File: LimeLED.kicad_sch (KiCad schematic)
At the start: 16 parts, among them CN1 HB9500-3, CN2 HB9500-3, U1 ESP32-DEVKITC-32D, U2 TPSM863257RDXR, U3 220k, U4 SN74AHCT125N

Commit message: add input protection and plotted schematic
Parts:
- added C7: 470uF 25v, Capacitor_THT:CP_Radial_D8.0mm_P3.50mm, symbol Device:C_Polarized
- added C8: 100nF 25v, Capacitor_SMD:C_0402_1005Metric, symbol Device:C_Small
- added F2: 500mA, easyeda2kicad:F1206, symbol easyeda2kicad:SMD1206B050TF_15
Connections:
- net +12V: now also F1.2, C7.1, C8.1, F2.2; no longer C1.2, C2.1, CN2.1, CN2.2, CN2.3, R1.1, U2.1 (VIN)
- net GND: now also C7.2, C8.2
- net at F1.1: now also CN2.1, CN2.2, CN2.3
- new net: C1.2, C2.1, F2.1, R1.1, U2.1 (VIN)
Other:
- moved on the sheet: CN1, CN2, F1

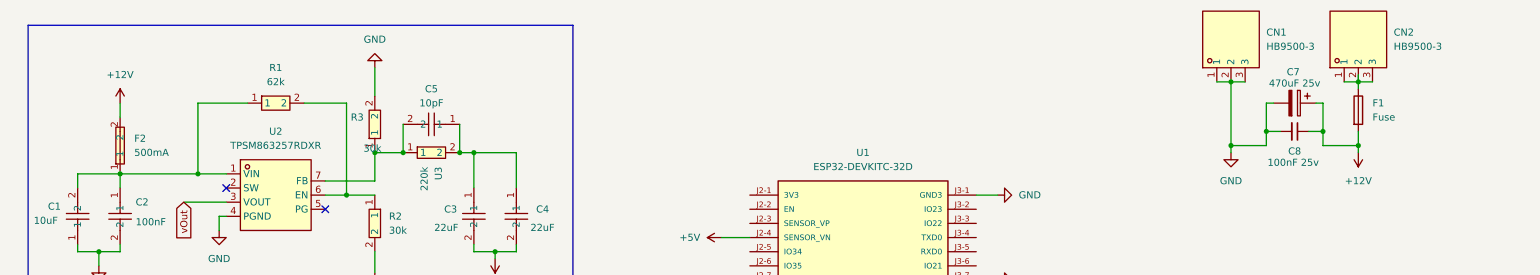
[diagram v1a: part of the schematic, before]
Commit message: wire connections
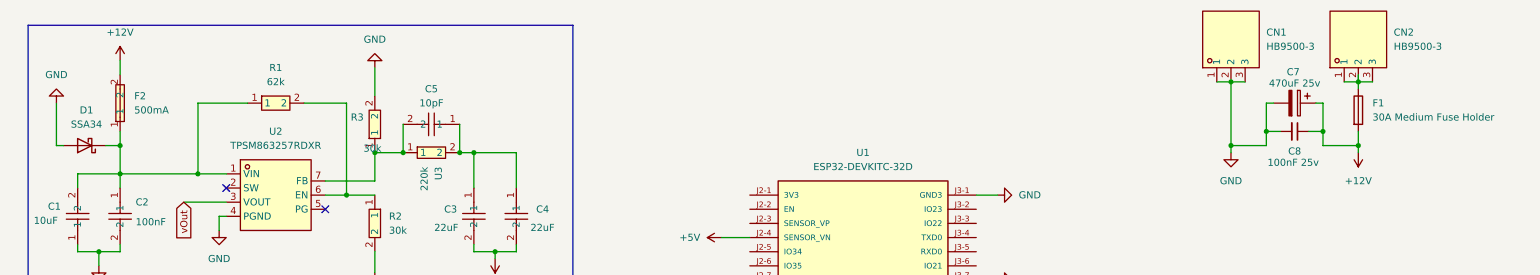
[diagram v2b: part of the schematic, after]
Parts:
- added D1: SSA34, Diode_SMD:D_SMA, symbol Device:D_Schottky
- F1: value Fuse -> 30A Medium Fuse Holder
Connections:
- net GND: now also D1.2 (A)
- net at C1.2, C2.1, F2.1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: now also D1.1 (K)
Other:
- moved on the sheet: F2
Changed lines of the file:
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@@
+	)
+	(junction
+		(at 35.56 43.18)
+		(diameter 0)
+		(color 0 0 0 0)
 	)
 	(junction
@@
 	(wire
 		(pts
+			(xy 24.13 43.18) (xy 25.4 43.18)
+		)
+		(stroke
+			(width 0)
+			(type default)
+		)
+	)
+	(wire
+		(pts
 			(xy 257.81 31.75) (xy 260.35 31.75)
 		)
@@
 	(wire
 		(pts
+			(xy 33.02 43.18) (xy 35.56 43.18)
+		)
+		(stroke
+			(width 0)
+			(type default)
+		)
+	)
+	(wire
+		(pts
 			(xy 106.68 60.96) (xy 106.68 62.23)
 		)
@@
 	(wire
 		(pts
+			(xy 35.56 27.94) (xy 35.56 30.48)
+		)
+		(stroke
+			(width 0)
+			(type default)
+		)
+	)
+	(wire
+		(pts
 			(xy 38.1 105.41) (xy 48.26 105.41)
 		)
@@
 	(wire
 		(pts
-			(xy 35.56 35.56) (xy 35.56 38.1)
-		)
-		(stroke
-			(width 0)
-			(type default)
-		)
-	)
-	(wire
-		(pts
 			(xy 73.66 105.41) (xy 78.74 105.41)
 		)
@@
 	(wire
 		(pts
+			(xy 24.13 35.56) (xy 24.13 43.18)
+		)
+		(stroke
+			(width 0)
+			(type default)
+		)
+	)
+	(wire
+		(pts
+			(xy 35.56 40.64) (xy 35.56 43.18)
+		)
+		(stroke
+			(width 0)
+			(type default)
+		)
+	)
+	(wire
+		(pts
 			(xy 49.53 35.56) (xy 58.42 35.56)
 		)
@@
 		(pts
 			(xy 43.18 102.87) (xy 43.18 110.49)
+		)
+		(stroke
+			(width 0)
+			(type default)
+		)
+	)
+	(wire
+		(pts
+			(xy 35.56 43.18) (xy 35.56 48.26)
 		)
 		(stroke
@@
 	(symbol
 		(lib_id "easyeda2kicad:SMD1206B050TF_15")
-		(at 35.56 43.18 90)
+		(at 35.56 35.56 90)
 		(unit 1)
 		(exclude_from_sim no)
@@
 		(fields_autoplaced yes)
 		(property "Reference" "F2"
-			(at 38.1 41.9099 90)
+			(at 38.1 34.2899 90)
 			(effects
 				(font
@@
 		)
 		(property "Value" "500mA"
-			(at 38.1 44.4499 90)
+			(at 38.1 36.8299 90)
 			(effects
 				(font
@@
 		)
 		(property "Footprint" "easyeda2kicad:F1206"
-			(at 43.18 43.18 0)
+			(at 43.18 35.56 0)
 			(effects
 				(font
@@
 		)
 		(property "Datasheet" "https://lcsc.com/product-detail/Surface-Mount-Fuses_0-5A-15V_C170165.html"
-			(at 45.72 43.18 0)
+			(at 45.72 35.56 0)
 			(effects
 				(font
@@
 		)
 		(property "Description" ""
-			(at 35.56 43.18 0)
+			(at 35.56 35.56 0)
 			(effects
 				(font
@@
 		)
 		(property "LCSC Part" "C170165"
-			(at 48.26 43.18 0)
+			(at 48.26 35.56 0)
 			(effects
 				(font
@@
 			)
 		)
-		(property "Value" "Fuse"
+		(property "Value" "30A Medium Fuse Holder"
 			(at 260.35 38.0999 0)
 			(effects
@@
 			)
 		)
-		(property "Description" "Fuse"
+		(property "Description" "Fuse https://www.aliexpress.com/item/33046363182.html?aff_fcid=27f0e0a0b700496bbda647752beed212-1654215773694-03622-_9iUXVp&tt=CPS_NORMAL&aff_fsk=_9iUXVp&afSmartRedirect=y&aff_fcid=e5dba592f4134194b19f09bf35b90000-1724109345417-07103-_9IbWU1&tt=CPS_NORMAL&aff_fsk=_9IbWU1&aff_platform=portals-tool&aff_trace_key=e5dba592f4134194b19f09bf35b90000-1724109345417-07103-_9IbWU1&afSmartRedirect=y"
 			(at 257.81 36.83 0)
 			(effects
@@
 	)
 	(symbol
+		(lib_id "Device:D_Schottky")
+		(at 29.21 43.18 180)
+		(unit 1)
+		(exclude_from_sim no)
+		(in_bom yes)
+		(on_board yes)
+		(dnp no)
+		(fields_autoplaced yes)
+		(property "Reference" "D1"
+			(at 29.5275 36.83 0)
+			(effects
+				(font
+					(size 1.27 1.27)
+				)
+			)
+		)
+		(property "Value" "SSA34"
+			(at 29.5275 39.37 0)
+			(effects
+				(font
+					(size 1.27 1.27)
+				)
+			)
+		)
+		(property "Footprint" "Diode_SMD:D_SMA"
+			(at 29.21 43.18 0)
+			(effects
+				(font
+					(size 1.27 1.27)
+				)
+				(hide yes)
+			)
+		)
+		(property "Datasheet" "~"
+			(at 29.21 43.18 0)
+			(effects
+				(font
+					(size 1.27 1.27)
+				)
+				(hide yes)
+			)
+		)
+		(property "Description" "Schottky diode"
+			(at 29.21 43.18 0)
+			(effects
+				(font
+					(size 1.27 1.27)
+				)
+				(hide yes)
+			)
+		)
+		(property "LCSC Part" "C5563753"
+			(at 29.21 43.18 0)
+			(effects
+				(font
+					(size 1.27 1.27)
+				)
+				(hide yes)
+			)
+		)
+		(pin "2"
+		)
+		(pin "1"
+		)
+		(instances
+			(project ""
+				(path "/8cd5c59d-c520-41d4-b0dd-a55cfcffecd3"
+					(reference "D1")
+					(unit 1)
+				)
+			)
+		)
+	)
+	(symbol
 		(lib_id "power:GND")
 		(at 234.95 44.45 0)
@@
 	(symbol
 		(lib_id "power:+12V")
-		(at 35.56 35.56 0)
+		(at 35.56 27.94 0)
 		(unit 1)
 		(exclude_from_sim no)
@@
 		(fields_autoplaced yes)
 		(property "Reference" "#PWR01"
-			(at 35.56 39.37 0)
+			(at 35.56 31.75 0)
 			(effects
 				(font
@@
 		)
 		(property "Value" "+12V"
-			(at 35.56 30.48 0)
+			(at 35.56 22.86 0)
 			(effects
 				(font
@@
 		)
 		(property "Footprint" ""
-			(at 35.56 35.56 0)
+			(at 35.56 27.94 0)
 			(effects
 				(font
@@
 		)
 		(property "Datasheet" ""
-			(at 35.56 35.56 0)
+			(at 35.56 27.94 0)
 			(effects
 				(font
@@
 		)
 		(property "Description" "Power symbol creates a global label with name \"+12V\""
-			(at 35.56 35.56 0)
+			(at 35.56 27.94 0)
 			(effects
 				(font
@@
 					(unit 1)
 				)
+			)
+		)
+	)
+	(symbol
+		(lib_id "power:GND")
+		(at 24.13 35.56 180)
+		(unit 1)
+		(exclude_from_sim no)
+		(in_bom yes)
+		(on_board yes)
+		(dnp no)
+		(fields_autoplaced yes)
+		(property "Reference" "#PWR016"
+			(at 24.13 29.21 0)
+			(effects
+				(font
+					(size 1.27 1.27)
+				)
+				(hide yes)
+			)
+		)
+		(property "Value" "GND"
+			(at 24.13 30.48 0)
+			(effects
+				(font
+					(size 1.27 1.27)
+				)
+			)
+		)
+		(property "Footprint" ""
+			(at 24.13 35.56 0)
+			(effects
+				(font
+					(size 1.27 1.27)
+				)
+				(hide yes)
+			)
+		)
+		(property "Datasheet" ""
+			(at 24.13 35.56 0)
+			(effects
+				(font
+					(size 1.27 1.27)
+				)
+				(hide yes)
+			)
+		)
+		(property "Description" "Power symbol creates a global label with name \"GND\" , ground"
+			(at 24.13 35.56 0)
+			(effects
+				(font
+					(size 1.27 1.27)
+				)
+				(hide yes)
+			)
+		)
+		(pin "1"
+		)
+		(instances
+			(project "LimeLED"
+				(path "/8cd5c59d-c520-41d4-b0dd-a55cfcffecd3"
+					(reference "#PWR016")
+					(unit 1)
+				)

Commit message: plot schematic
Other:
- note added: "Power in"
- moved on the sheet: C7, C8, CN1, CN2, F1

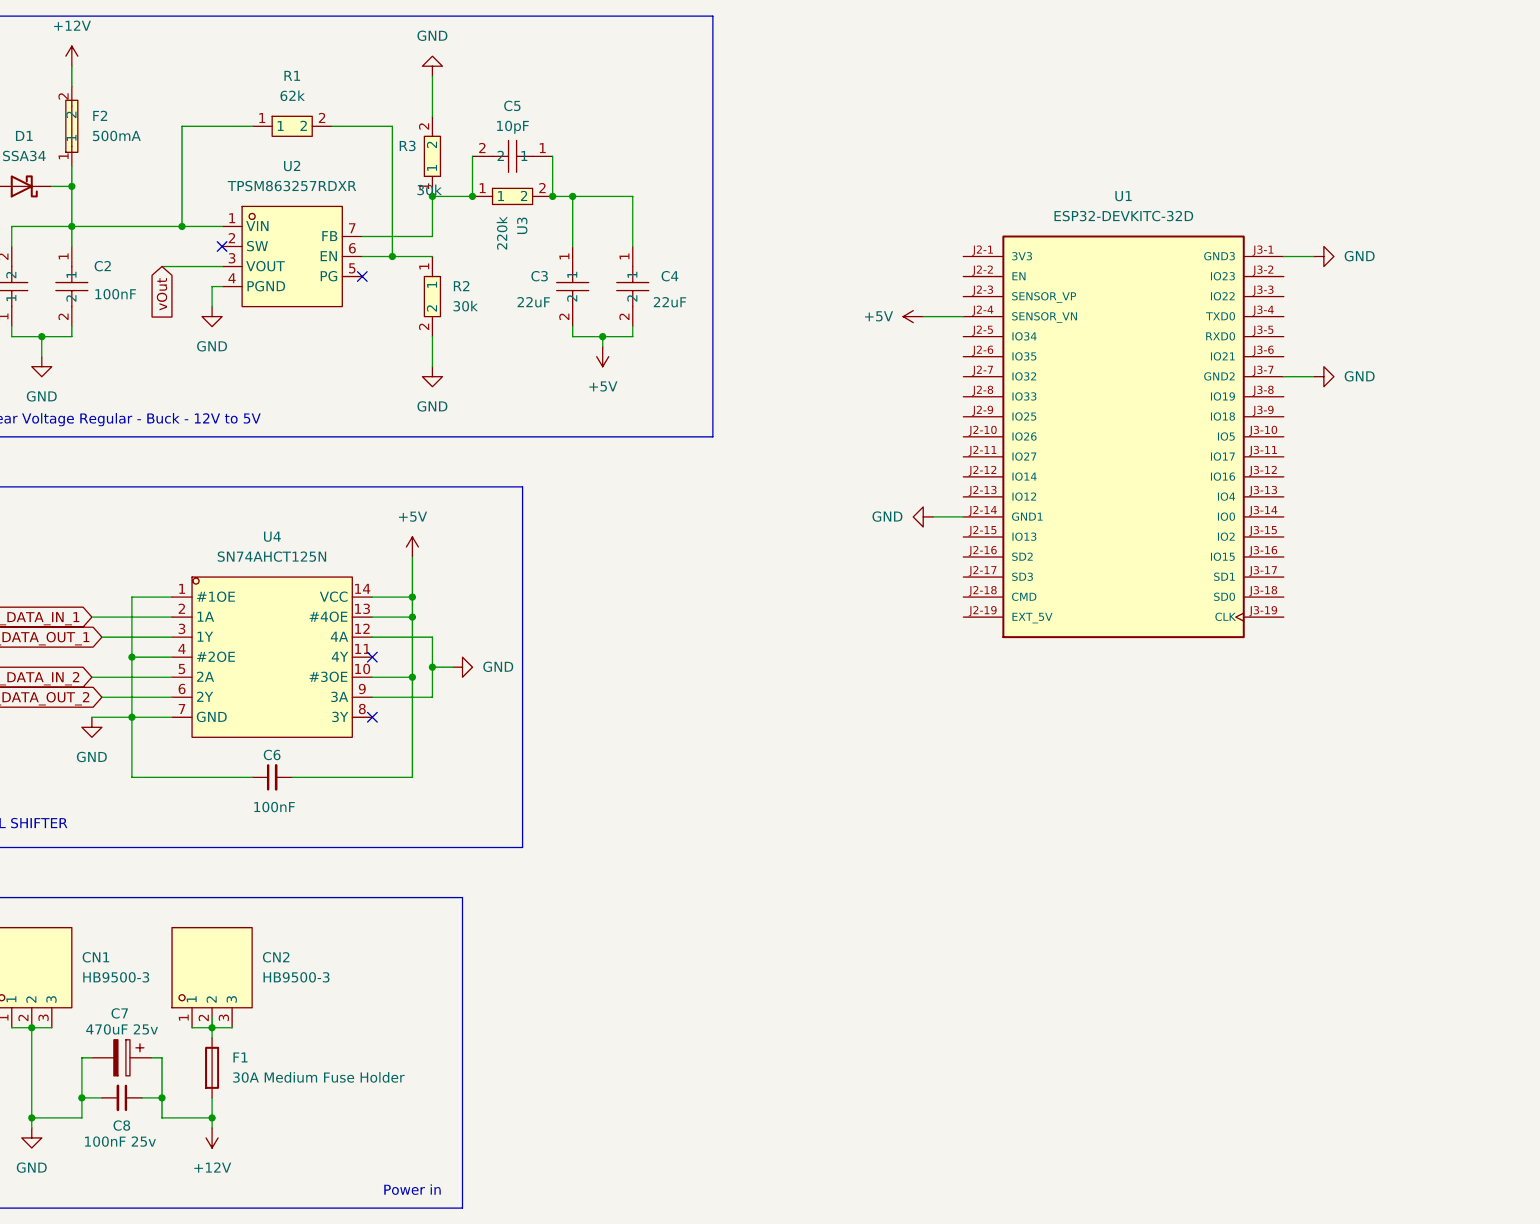
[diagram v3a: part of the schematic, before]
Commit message: add relay
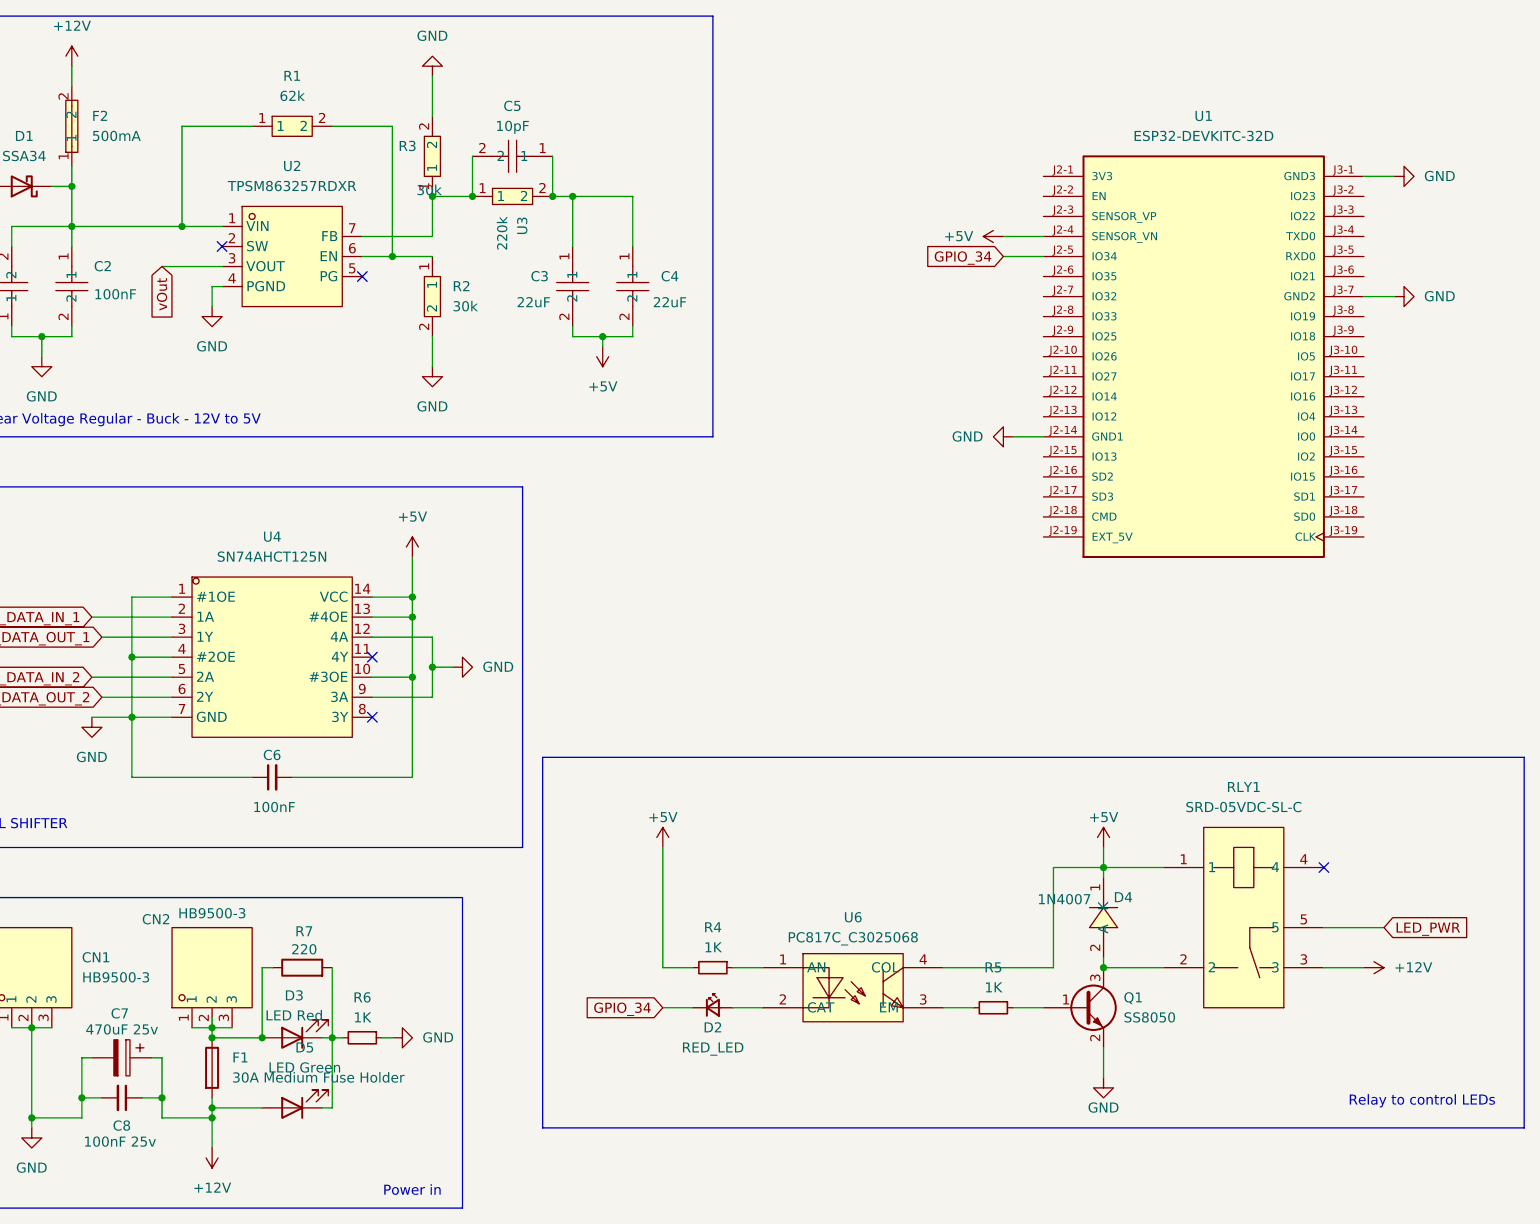
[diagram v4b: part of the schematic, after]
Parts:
- added D2: RED_LED, LED_SMD:LED_0805_2012Metric_Pad1.15x1.40mm_HandSolder, symbol Device:LED_Small
- added D3: LED Red, LED_THT:LED_D3.0mm_Horizontal_O6.35mm_Z10.0mm, symbol Device:LED
- added D4: 1N4007, easyeda2kicad:SMA_L4.3-W2.5-LS5.0-RD, symbol easyeda2kicad:1N4007_C727081
- added D5: LED Green, LED_THT:LED_D3.0mm_Horizontal_O6.35mm_Z10.0mm, symbol Device:LED
- added Q1: SS8050, Package_TO_SOT_SMD:SOT-23, symbol Device:Q_NPN_BEC
- added R4, R5, R6: 1K, Resistor_SMD:R_0402_1005Metric, symbol Device:R_Small
- added R7: 220, Resistor_SMD:R_1206_3216Metric, symbol Device:R
- added RLY1: SRD-05VDC-SL-C, easyeda2kicad:RELAY-TH_SRD-XXVDC-XL-C, symbol easyeda2kicad:SRD-05VDC-SL-C
- added U6: PC817C_C3025068, easyeda2kicad:DIP-4_L4.6-W6.5-P2.54-LS7.6-BL, symbol easyeda2kicad:PC817C_C3025068
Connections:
- net +12V: now also D5.2 (A), RLY1.3
- net +5V: now also D4.1 (K), R4.2, RLY1.1, U6.4 (COL)
- net GND: now also Q1.2 (E), R6.1
- net at CN2.1, CN2.2, CN2.3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: now also D3.2 (A), R7.1
- net GPIO_34: now reaches U1.J2-5 (IO34)
- net GPIO_34: now also D2.1 (K)
- new net: D4.2 (A), Q1.3 (C), RLY1.2
- new net: D3.1 (K), D5.1 (K), R6.2, R7.2
- new net: Q1.1 (B), R5.1
- new net: R5.2, U6.3 (EM)
- new net: R4.1, U6.1 (AN)
- new net: D2.2 (A), U6.2 (CAT)
- new net LED_PWR: RLY1.5
- no-connect marks 4 -> 5
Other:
- note added: "Relay to control LEDs"
- moved on the sheet: U1

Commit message: add 64p PSU connector
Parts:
- removed F1: 30A Medium Fuse Holder, Custom_footprint:Ebay-Fuse-holder-04mmX15mm-black-auto-fuse-dingus, symbol Device:Fuse
- added C9: 470uF 25v, Capacitor_THT:CP_Radial_D8.0mm_P3.50mm, symbol Device:C_Polarized
- added CN3: ER64BGFBK, easyeda2kicad:CONN-TH_64P-P2.54_ER64BGFBK, symbol easyeda2kicad:ER64BGFBK
- added F5: 10A Medium Fuse Holder, Custom_footprint:Ebay-Fuse-holder-04mmX15mm-black-auto-fuse-dingus, symbol Device:Fuse
- added F6, F7: 10A, Custom_footprint:Ebay-Fuse-holder-04mmX15mm-black-auto-fuse-dingus, symbol Device:Fuse
- added R9: 21k, Resistor_SMD:R_0603_1608Metric, symbol Device:R
- added U5, U7: MBR20100DT, easyeda2kicad:TO-252-2_L6.5-W6.1-P4.58-LS10.0-BL, symbol easyeda2kicad:MBR20100DT_C3011043
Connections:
- net +12V: now also CN3.64; no longer C7.1, C8.1, D5.2 (A)
- net GND: now also CN3.33, CN3.34, CN3.35, CN3.36, CN3.37, CN3.38, CN3.39, CN3.40, CN3.41, CN3.42, CN3.43, CN3.44, CN3.45, CN3.46, CN3.47, CN3.48, CN3.49, CN3.50, CN3.51, CN3.52; no longer C7.2, C8.2
- new net: C7.1, C7.2
- new net: CN3.56, R9.2
- new net: CN3.58, R9.1
- new net: D3.2 (A), R7.1
- new net: U5.1 (A), U5.3 (A), U7.1 (A), U7.3 (A)
- new net +12V #1: CN2.1, CN3.10, CN3.12, CN3.14, CN3.16, CN3.18, CN3.2, CN3.20, CN3.4, CN3.6, CN3.8, F5.1
- new net +12V #2: CN2.2, CN3.1, CN3.11, CN3.13, CN3.15, CN3.17, CN3.19, CN3.21, CN3.3, CN3.5, CN3.7, CN3.9, F6.1
- new net +12V #3: CN2.3, CN3.22, CN3.23, CN3.24, CN3.25, CN3.26, CN3.27, CN3.28, CN3.29, CN3.30, CN3.31, CN3.32, F7.1
- no-connect marks 5 -> 13
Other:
- note added: "Reverse Polarity, Filtering, Fuse Monitoring"
- moved on the sheet: C7, C8, CN1, CN2, D2, D3, D4, D5, Q1, R4, R5, R6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

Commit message: finish input power connector
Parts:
- removed D3: LED Red, LED_THT:LED_D3.0mm_Horizontal_O6.35mm_Z10.0mm, symbol Device:LED
- removed D5: LED Green, LED_THT:LED_D3.0mm_Horizontal_O6.35mm_Z10.0mm, symbol Device:LED
- removed F7: 10A, Custom_footprint:Ebay-Fuse-holder-04mmX15mm-black-auto-fuse-dingus, symbol Device:Fuse
- removed R7: 220, Resistor_SMD:R_1206_3216Metric, symbol Device:R
- added C10: 10uF, Capacitor_SMD:C_0603_1608Metric, symbol Device:C_Small
- added D3: RED_LED, LED_SMD:LED_0805_2012Metric_Pad1.15x1.40mm_HandSolder, symbol Device:LED_Small
- added D5: 1N4007, easyeda2kicad:SMA_L4.3-W2.5-LS5.0-RD, symbol easyeda2kicad:1N4007_C727081
- added D6: LED Red, Custom_footprint:LED_D3.0mm_Horizontal_O6.35mm_Z10.0mm, symbol Device:LED
- added F1: 10A, Custom_footprint:Ebay-Fuse-holder-04mmX15mm-black-auto-fuse-dingus, symbol Device:Fuse
- added Q2: SS8050, Package_TO_SOT_SMD:SOT-23, symbol Device:Q_NPN_BEC
- added R7: 1K, Resistor_SMD:R_0402_1005Metric, symbol Device:R_Small
- added R8: 2.2k, Resistor_SMD:R_0603_1608Metric, symbol Device:R
- added RLY2: SRD-05VDC-SL-C, easyeda2kicad:RELAY-TH_SRD-XXVDC-XL-C, symbol easyeda2kicad:SRD-05VDC-SL-C
- added U10, U11, U9: SD103AW, easyeda2kicad:SOD-123_L2.8-W1.8-LS3.7-RD, symbol easyeda2kicad:SD103AW_C5345965
- added U12: PC817C_C3025068, easyeda2kicad:DIP-4_L4.6-W6.5-P2.54-LS7.6-BL, symbol easyeda2kicad:PC817C_C3025068
- added U8: MBR20100DT, easyeda2kicad:TO-252-2_L6.5-W6.1-P4.58-LS10.0-BL, symbol easyeda2kicad:MBR20100DT_C3011043
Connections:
- net +12V: now also C7.1, C8.1, C9.1, F5.2, F6.2, C10.1, F1.2, RLY2.3
- net +12V #1: now also U5.1 (A), U5.3 (A); no longer F5.1
- net +12V #2: now also U8.1 (A), U8.3 (A); no longer F6.1
- net +12V #3: now also U7.1 (A), U7.3 (A)
- net +5V: now also R6.2, U1.J2-19 (EXT_5V), D5.1 (K), RLY2.1, U12.4 (COL); no longer U1.J2-4 (SENSOR_VN)
- net GND: now also C7.2, C8.2, C9.2, C10.2, D6.1 (K), Q2.2 (E); no longer R6.1
- net LED_DATA_IN_1: now also U1.J3-13 (IO4)
- net LED_DATA_IN_2: now also U1.J3-15 (IO2)
- net LED_PWR: now also RLY2.5
- net at U7.2 (K): now also F1.1, U11.2 (A)
- net at U5.2 (K): now also F5.1, U9.2 (A)
- net RELAY: now reaches U1.J2-13 (IO12)
- net RELAY: now also D2.1 (K), D3.1 (K)
- net GPIO_34: no longer names the net of U1.J2-5 (IO34)
- net GPIO_34: no longer D2.1 (K)
- new net: D6.2 (A), R8.2
- new net: F6.1, U10.2 (A), U8.2 (K)
- new net: R8.1, U10.1 (C), U11.1 (C), U9.1 (C)
- new net: R6.1, U12.1 (AN)
- new net: D3.2 (A), U12.2 (CAT)
- new net: R7.2, U12.3 (EM)
- new net: Q2.1 (B), R7.1
- new net: D5.2 (A), Q2.3 (C), RLY2.2
- no-connect marks 13 -> 14
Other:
- note added: "https://makenotes.de/2020/04/turning-on-a-hp-dps-750rb-server-power-supply/"
- moved on the sheet: C6, C7, C8, C9, CN1, CN2, CN3, D2, D4, F5, F6, Q1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
